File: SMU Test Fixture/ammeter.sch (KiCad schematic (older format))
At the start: 42 parts, among them K10 Integrator Reset, K5 3x Gain Enable, K6 Shunt Select, K7 Sense Select, K8 I/V Mode Select, K9 Shunt/Sense Select, U1 OPA189, U2 OPA551U, U3 OPA189, U4 OPA1611, U5 OPA192, U6 OPA192

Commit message: Add footprints for low precision/low power parts.
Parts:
- C1, C10, C11, C12, C13, C15, C2, C3, C4, C5, C6, C7, C8, C9: footprint (none) -> Capacitor_SMD:C_0805_2012Metric_Pad1.18x1.45mm_HandSolder
- R10, R12, R13, R14, R15, R16, R17, R18, R19, R8: footprint (none) -> Resistor_SMD:R_0805_2012Metric_Pad1.20x1.40mm_HandSolder
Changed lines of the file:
@@
 F 0 "C1" H 1092 946 50  0000 L CNN
 F 1 "100n" H 1092 855 50  0000 L CNN
-F 2 "" H 1000 900 50  0001 C CNN
+F 2 "Capacitor_SMD:C_0805_2012Metric_Pad1.18x1.45mm_HandSolder" H 1000 900 50  0001 C CNN
 F 3 "~" H 1000 900 50  0001 C CNN
 	1    1000 900
@@
 F 0 "C2" H 1092 1346 50  0000 L CNN
 F 1 "100n" H 1092 1255 50  0000 L CNN
-F 2 "" H 1000 1300 50  0001 C CNN
+F 2 "Capacitor_SMD:C_0805_2012Metric_Pad1.18x1.45mm_HandSolder" H 1000 1300 50  0001 C CNN
 F 3 "~" H 1000 1300 50  0001 C CNN
 	1    1000 1300
@@
 F 0 "R17" V 7895 3900 50  0000 C CNN
 F 1 "1M" V 7986 3900 50  0000 C CNN
-F 2 "" H 8100 3900 50  0001 C CNN
+F 2 "Resistor_SMD:R_0805_2012Metric_Pad1.20x1.40mm_HandSolder" H 8100 3900 50  0001 C CNN
 F 3 "~" H 8100 3900 50  0001 C CNN
 	1    8100 3900
@@
 F 0 "R16" V 7845 2450 50  0000 C CNN
 F 1 "1M" V 7936 2450 50  0000 C CNN
-F 2 "" H 8050 2450 50  0001 C CNN
+F 2 "Resistor_SMD:R_0805_2012Metric_Pad1.20x1.40mm_HandSolder" H 8050 2450 50  0001 C CNN
 F 3 "~" H 8050 2450 50  0001 C CNN
 	1    8050 2450
@@
 F 0 "R10" H 1700 3100 50  0000 C CNN
 F 1 "56K" H 1700 3000 50  0000 C CNN
-F 2 "" H 1800 3100 50  0001 C CNN
+F 2 "Resistor_SMD:R_0805_2012Metric_Pad1.20x1.40mm_HandSolder" H 1800 3100 50  0001 C CNN
 F 3 "~" H 1800 3100 50  0001 C CNN
 	1    1800 3100
@@
 F 0 "C13" H 2692 4046 50  0000 L CNN
 F 1 "33p" H 2692 3955 50  0000 L CNN
-F 2 "" H 2600 4000 50  0001 C CNN
+F 2 "Capacitor_SMD:C_0805_2012Metric_Pad1.18x1.45mm_HandSolder" H 2600 4000 50  0001 C CNN
 F 3 "~" H 2600 4000 50  0001 C CNN
 	1    2600 4000
@@
 F 0 "R8" V 945 4550 50  0000 C CNN
 F 1 "5.9K" V 1036 4550 50  0000 C CNN
-F 2 "" H 1150 4550 50  0001 C CNN
+F 2 "Resistor_SMD:R_0805_2012Metric_Pad1.20x1.40mm_HandSolder" H 1150 4550 50  0001 C CNN
 F 3 "~" H 1150 4550 50  0001 C CNN
 	1    1150 4550
@@
 F 0 "R12" V 3850 3800 50  0000 C CNN
 F 1 "11.8K" V 3636 3800 50  0000 C CNN
-F 2 "" H 3750 3800 50  0001 C CNN
+F 2 "Resistor_SMD:R_0805_2012Metric_Pad1.20x1.40mm_HandSolder" H 3750 3800 50  0001 C CNN
 F 3 "~" H 3750 3800 50  0001 C CNN
 	1    3750 3800
@@
 F 0 "R15" V 6845 5600 50  0000 C CNN
 F 1 "14.7K" V 6936 5600 50  0000 C CNN
-F 2 "" H 7050 5600 50  0001 C CNN
+F 2 "Resistor_SMD:R_0805_2012Metric_Pad1.20x1.40mm_HandSolder" H 7050 5600 50  0001 C CNN
 F 3 "~" H 7050 5600 50  0001 C CNN
 	1    7050 5600
@@
 F 0 "C15" V 6821 5950 50  0000 C CNN
 F 1 "6.2p" V 6912 5950 50  0000 C CNN
-F 2 "" H 7050 5950 50  0001 C CNN
+F 2 "Capacitor_SMD:C_0805_2012Metric_Pad1.18x1.45mm_HandSolder" H 7050 5950 50  0001 C CNN
 F 3 "~" H 7050 5950 50  0001 C CNN
 	1    7050 5950
@@
 F 0 "C3" H 1392 946 50  0000 L CNN
 F 1 "100n" H 1392 855 50  0000 L CNN
-F 2 "" H 1300 900 50  0001 C CNN
+F 2 "Capacitor_SMD:C_0805_2012Metric_Pad1.18x1.45mm_HandSolder" H 1300 900 50  0001 C CNN
 F 3 "~" H 1300 900 50  0001 C CNN
 	1    1300 900
@@
 F 0 "C5" H 1692 946 50  0000 L CNN
 F 1 "100n" H 1692 855 50  0000 L CNN
-F 2 "" H 1600 900 50  0001 C CNN
+F 2 "Capacitor_SMD:C_0805_2012Metric_Pad1.18x1.45mm_HandSolder" H 1600 900 50  0001 C CNN
 F 3 "~" H 1600 900 50  0001 C CNN
 	1    1600 900
@@
 F 0 "C7" H 1992 946 50  0000 L CNN
 F 1 "100n" H 1992 855 50  0000 L CNN
-F 2 "" H 1900 900 50  0001 C CNN
+F 2 "Capacitor_SMD:C_0805_2012Metric_Pad1.18x1.45mm_HandSolder" H 1900 900 50  0001 C CNN
 F 3 "~" H 1900 900 50  0001 C CNN
 	1    1900 900
@@
 F 0 "C9" H 2292 946 50  0000 L CNN
 F 1 "100n" H 2292 855 50  0000 L CNN
-F 2 "" H 2200 900 50  0001 C CNN
+F 2 "Capacitor_SMD:C_0805_2012Metric_Pad1.18x1.45mm_HandSolder" H 2200 900 50  0001 C CNN
 F 3 "~" H 2200 900 50  0001 C CNN
 	1    2200 900
@@
 F 0 "C11" H 2592 946 50  0000 L CNN
 F 1 "100n" H 2592 855 50  0000 L CNN
-F 2 "" H 2500 900 50  0001 C CNN
+F 2 "Capacitor_SMD:C_0805_2012Metric_Pad1.18x1.45mm_HandSolder" H 2500 900 50  0001 C CNN
 F 3 "~" H 2500 900 50  0001 C CNN
 	1    2500 900
@@
 F 0 "C4" H 1392 1346 50  0000 L CNN
 F 1 "100n" H 1392 1255 50  0000 L CNN
-F 2 "" H 1300 1300 50  0001 C CNN
+F 2 "Capacitor_SMD:C_0805_2012Metric_Pad1.18x1.45mm_HandSolder" H 1300 1300 50  0001 C CNN
 F 3 "~" H 1300 1300 50  0001 C CNN
 	1    1300 1300
@@
 F 0 "C6" H 1692 1346 50  0000 L CNN
 F 1 "100n" H 1692 1255 50  0000 L CNN
-F 2 "" H 1600 1300 50  0001 C CNN
+F 2 "Capacitor_SMD:C_0805_2012Metric_Pad1.18x1.45mm_HandSolder" H 1600 1300 50  0001 C CNN
 F 3 "~" H 1600 1300 50  0001 C CNN
 	1    1600 1300
@@
 F 0 "C8" H 1992 1346 50  0000 L CNN
 F 1 "100n" H 1992 1255 50  0000 L CNN
-F 2 "" H 1900 1300 50  0001 C CNN
+F 2 "Capacitor_SMD:C_0805_2012Metric_Pad1.18x1.45mm_HandSolder" H 1900 1300 50  0001 C CNN
 F 3 "~" H 1900 1300 50  0001 C CNN
 	1    1900 1300
@@
 F 0 "C10" H 2292 1346 50  0000 L CNN
 F 1 "100n" H 2292 1255 50  0000 L CNN
-F 2 "" H 2200 1300 50  0001 C CNN
+F 2 "Capacitor_SMD:C_0805_2012Metric_Pad1.18x1.45mm_HandSolder" H 2200 1300 50  0001 C CNN
 F 3 "~" H 2200 1300 50  0001 C CNN
 	1    2200 1300
@@
 F 0 "C12" H 2592 1346 50  0000 L CNN
 F 1 "100n" H 2592 1255 50  0000 L CNN
-F 2 "" H 2500 1300 50  0001 C CNN
+F 2 "Capacitor_SMD:C_0805_2012Metric_Pad1.18x1.45mm_HandSolder" H 2500 1300 50  0001 C CNN
 F 3 "~" H 2500 1300 50  0001 C CNN
 	1    2500 1300
@@
 F 0 "R18" V 9200 2300 50  0000 C CNN
 F 1 "5K" V 9400 2300 50  0000 C CNN
-F 2 "" H 9300 2300 50  0001 C CNN
+F 2 "Resistor_SMD:R_0805_2012Metric_Pad1.20x1.40mm_HandSolder" H 9300 2300 50  0001 C CNN
 F 3 "~" H 9300 2300 50  0001 C CNN
 	1    9300 2300
@@
 F 0 "R19" V 9250 3750 50  0000 C CNN
 F 1 "5K" V 9450 3750 50  0000 C CNN
-F 2 "" H 9350 3750 50  0001 C CNN
+F 2 "Resistor_SMD:R_0805_2012Metric_Pad1.20x1.40mm_HandSolder" H 9350 3750 50  0001 C CNN
 F 3 "~" H 9350 3750 50  0001 C CNN
 	1    9350 3750
@@
 F 0 "R14" V 5800 5950 50  0000 C CNN
 F 1 "150R" V 5900 5950 50  0000 C CNN
-F 2 "" H 6000 5950 50  0001 C CNN
+F 2 "Resistor_SMD:R_0805_2012Metric_Pad1.20x1.40mm_HandSolder" H 6000 5950 50  0001 C CNN
 F 3 "~" H 6000 5950 50  0001 C CNN
 	1    6000 5950
@@
 F 0 "R13" V 5800 5600 50  0000 C CNN
 F 1 "14.7K" V 5900 5600 50  0000 C CNN
-F 2 "" H 6000 5600 50  0001 C CNN
+F 2 "Resistor_SMD:R_0805_2012Metric_Pad1.20x1.40mm_HandSolder" H 6000 5600 50  0001 C CNN
 F 3 "~" H 6000 5600 50  0001 C CNN
 	1    6000 5600

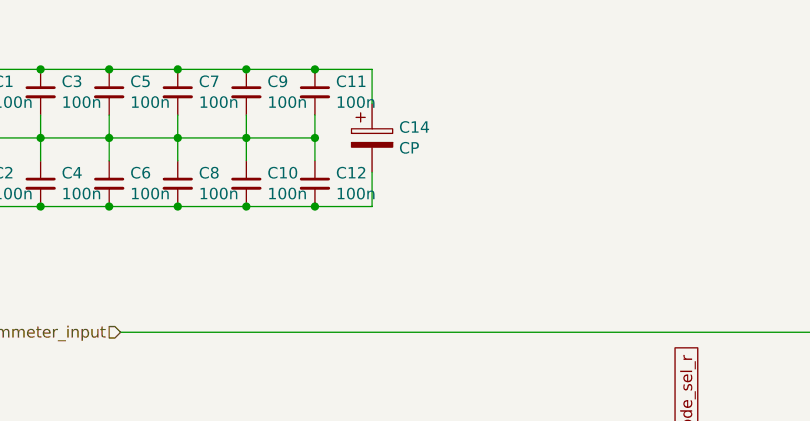
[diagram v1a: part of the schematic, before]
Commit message: More footprints added.
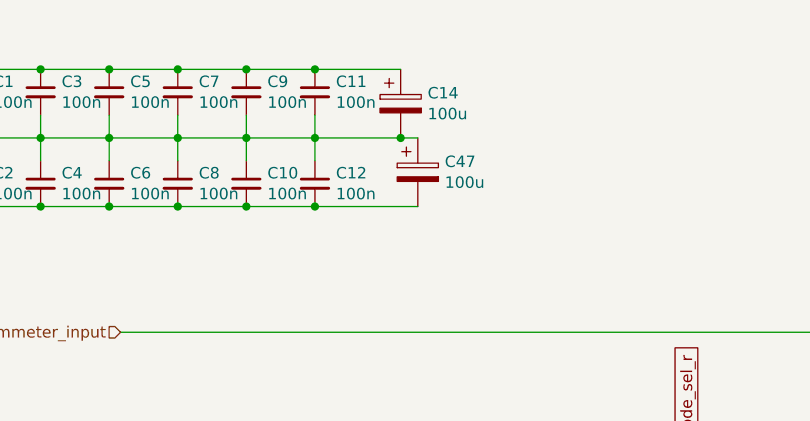
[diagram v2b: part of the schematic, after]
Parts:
- added C47: 100u, Capacitor_SMD:CP_Elec_8x10, symbol Device:CP
- C14: value CP -> 100u; footprint (none) -> Capacitor_SMD:CP_Elec_8x10; PN (none) -> UCD1V101MNL1GS
- C15: footprint Capacitor_SMD:C_0805_2012Metric_Pad1.18x1.45mm_HandSolder -> Capacitor_SMD:C_0603_1608Metric_Pad1.08x0.95mm_HandSolder; PN (none) -> GRM0335C1H6R2BA01D
- C16, C17: footprint (none) -> Capacitor_THT:C_Rect_L18.0mm_W11.0mm_P15.00mm_FKS3_FKP3; PN (none) -> ECW-FD2W105JC
- R11: footprint (none) -> Resistor_SMD:R_0805_2012Metric_Pad1.20x1.40mm_HandSolder; PN (none) -> ERA-6ARW103V
- R13, R15: footprint Resistor_SMD:R_0805_2012Metric_Pad1.20x1.40mm_HandSolder -> Resistor_SMD:R_1206_3216Metric_Pad1.30x1.75mm_HandSolder; PN (none) -> ERA-8ARW1472V
- R14: footprint Resistor_SMD:R_0805_2012Metric_Pad1.20x1.40mm_HandSolder -> Resistor_SMD:R_0603_1608Metric_Pad0.98x0.95mm_HandSolder; PN (none) -> RG1608N-151-W-T1
- R7: footprint (none) -> eaton:CSM_Vishay_Shunt_4term; PN (none) -> Y14870R01000B9R
- R9: footprint (none) -> Resistor_SMD:R_0805_2012Metric_Pad1.20x1.40mm_HandSolder; PN (none) -> RNCF0805AKT10R0
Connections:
- net -15V: now also C47.2; no longer C14.2
- net GND: now also C14.2, C47.1
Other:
- moved on the sheet: C14
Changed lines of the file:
@@
 F 0 "R11" H 2000 6200 50  0000 L CNN
 F 1 "10K" H 2000 6100 50  0000 L CNN
-F 2 "" H 1950 5850 50  0001 C CNN
+F 2 "Resistor_SMD:R_0805_2012Metric_Pad1.20x1.40mm_HandSolder" H 1950 5850 50  0001 C CNN
 F 3 "~" H 1950 5850 50  0001 C CNN
+F 4 " ERA-6ARW103V" H 1950 5850 50  0001 C CNN "PN"
 	1    1950 5850
 	-1   0    0    -1
@@
 F 0 "R9" H 1500 6200 50  0000 L CNN
 F 1 "10R" H 1500 6100 50  0000 L CNN
-F 2 "" H 1450 5850 50  0001 C CNN
+F 2 "Resistor_SMD:R_0805_2012Metric_Pad1.20x1.40mm_HandSolder" H 1450 5850 50  0001 C CNN
 F 3 "~" H 1450 5850 50  0001 C CNN
+F 4 "RNCF0805AKT10R0" H 1450 5850 50  0001 C CNN "PN"
 	1    1450 5850
 	-1   0    0    -1
@@
 F 0 "C17" V 8450 3300 50  0000 C CNN
 F 1 "1u" V 8650 3300 50  0000 C CNN
-F 2 "" H 8550 3300 50  0001 C CNN
+F 2 "Capacitor_THT:C_Rect_L18.0mm_W11.0mm_P15.00mm_FKS3_FKP3" H 8550 3300 50  0001 C CNN
 F 3 "~" H 8550 3300 50  0001 C CNN
+F 4 " ECW-FD2W105JC " V 8550 3300 50  0001 C CNN "PN"
 	1    8550 3300
 	0    1    1    0
@@
 F 0 "R7" H 1250 6300 50  0000 R CNN
 F 1 "0R01" H 1300 6200 50  0000 R CNN
-F 2 "" V 1030 5900 50  0001 C CNN
+F 2 "eaton:CSM_Vishay_Shunt_4term" V 1030 5900 50  0001 C CNN
 F 3 "~" H 1100 5900 50  0001 C CNN
+F 4 "Y14870R01000B9R" H 1100 5900 50  0001 C CNN "PN"
 	1    1100 5900
 	-1   0    0    -1
@@
 F 0 "R15" V 6845 5600 50  0000 C CNN
 F 1 "14.7K" V 6936 5600 50  0000 C CNN
-F 2 "Resistor_SMD:R_0805_2012Metric_Pad1.20x1.40mm_HandSolder" H 7050 5600 50  0001 C CNN
+F 2 "Resistor_SMD:R_1206_3216Metric_Pad1.30x1.75mm_HandSolder" H 7050 5600 50  0001 C CNN
 F 3 "~" H 7050 5600 50  0001 C CNN
+F 4 "ERA-8ARW1472V" V 7050 5600 50  0001 C CNN "PN"
 	1    7050 5600
 	0    1    1    0
@@
 F 0 "C15" V 6821 5950 50  0000 C CNN
 F 1 "6.2p" V 6912 5950 50  0000 C CNN
-F 2 "Capacitor_SMD:C_0805_2012Metric_Pad1.18x1.45mm_HandSolder" H 7050 5950 50  0001 C CNN
+F 2 "Capacitor_SMD:C_0603_1608Metric_Pad1.08x0.95mm_HandSolder" H 7050 5950 50  0001 C CNN
 F 3 "~" H 7050 5950 50  0001 C CNN
+F 4 "GRM0335C1H6R2BA01D" V 7050 5950 50  0001 C CNN "PN"
 	1    7050 5950
 	0    1    1    0
@@
 F 0 "C16" V 8400 1850 50  0000 C CNN
 F 1 "1u" V 8600 1850 50  0000 C CNN
-F 2 "" H 8500 1850 50  0001 C CNN
+F 2 "Capacitor_THT:C_Rect_L18.0mm_W11.0mm_P15.00mm_FKS3_FKP3" H 8500 1850 50  0001 C CNN
 F 3 "~" H 8500 1850 50  0001 C CNN
+F 4 " ECW-FD2W105JC " V 8500 1850 50  0001 C CNN "PN"
 	1    8500 1850
 	0    1    1    0
@@
 L Device:CP C14
 U 1 1 60ECEBF3
-P 2750 1100
-F 0 "C14" H 2868 1146 50  0000 L CNN
-F 1 "CP" H 2868 1055 50  0000 L CNN
-F 2 "" H 2788 950 50  0001 C CNN
-F 3 "~" H 2750 1100 50  0001 C CNN
-	1    2750 1100
-	1    0    0    -1
-$EndComp
-Wire Wire Line
-	2750 800  2750 950
-Wire Wire Line
-	2750 1400 2750 1250
+P 2875 950
+F 0 "C14" H 2993 996 50  0000 L CNN
+F 1 "100u" H 2993 905 50  0000 L CNN
+F 2 "Capacitor_SMD:CP_Elec_8x10" H 2913 800 50  0001 C CNN
+F 3 "~" H 2875 950 50  0001 C CNN
+F 4 "UCD1V101MNL1GS" H 2875 950 50  0001 C CNN "PN"
+	1    2875 950
+	1    0    0    -1
+$EndComp
 Wire Wire Line
 	1000 800  1300 800
@@
 $EndComp
 Connection ~ 2500 800
-Wire Wire Line
-	2500 800  2750 800
 $Comp
 L Device:C_Small C4
@@
 $EndComp
 Connection ~ 2500 1400
-Wire Wire Line
-	2500 1400 2750 1400
 $Comp
 L power:-15V #PWR012
@@
 F 0 "R14" V 5800 5950 50  0000 C CNN
 F 1 "150R" V 5900 5950 50  0000 C CNN
-F 2 "Resistor_SMD:R_0805_2012Metric_Pad1.20x1.40mm_HandSolder" H 6000 5950 50  0001 C CNN
+F 2 "Resistor_SMD:R_0603_1608Metric_Pad0.98x0.95mm_HandSolder" H 6000 5950 50  0001 C CNN
 F 3 "~" H 6000 5950 50  0001 C CNN
+F 4 "RG1608N-151-W-T1" V 6000 5950 50  0001 C CNN "PN"
 	1    6000 5950
 	0    1    1    0
@@
 F 0 "R13" V 5800 5600 50  0000 C CNN
 F 1 "14.7K" V 5900 5600 50  0000 C CNN
-F 2 "Resistor_SMD:R_0805_2012Metric_Pad1.20x1.40mm_HandSolder" H 6000 5600 50  0001 C CNN
+F 2 "Resistor_SMD:R_1206_3216Metric_Pad1.30x1.75mm_HandSolder" H 6000 5600 50  0001 C CNN
 F 3 "~" H 6000 5600 50  0001 C CNN
+F 4 "ERA-8ARW1472V" V 6000 5600 50  0001 C CNN "PN"
 	1    6000 5600
 	0    1    1    0
@@
 	1    0    0    -1
 $EndComp
+$Comp
+L Device:CP C47
+U 1 1 6014511A
+P 2950 1250
+F 0 "C47" H 3068 1296 50  0000 L CNN
+F 1 "100u" H 3068 1205 50  0000 L CNN
+F 2 "Capacitor_SMD:CP_Elec_8x10" H 2988 1100 50  0001 C CNN
+F 3 "~" H 2950 1250 50  0001 C CNN
+F 4 "UCD1V101MNL1GS" H 2950 1250 50  0001 C CNN "PN"
+	1    2950 1250
+	1    0    0    -1
+$EndComp
+Wire Wire Line
+	2500 1400 2950 1400
+Wire Wire Line
+	2500 1100 2875 1100
+Wire Wire Line
+	2875 1100 2950 1100
+Connection ~ 2875 1100
+Wire Wire Line
+	2500 800  2875 800
 $EndSCHEMATC

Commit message: Footprint updates
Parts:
- C1, C10, C11, C12, C2, C3, C4, C5, C6, C7, C8, C9: footprint Capacitor_SMD:C_0805_2012Metric_Pad1.18x1.45mm_HandSolder -> Capacitor_SMD:C_1206_3216Metric_Pad1.33x1.80mm_HandSolder; PN (none) -> CGA5L2C0G1H104J160AA
- C13: footprint Capacitor_SMD:C_0805_2012Metric_Pad1.18x1.45mm_HandSolder -> Capacitor_SMD:C_0201_0603Metric_Pad0.64x0.40mm_HandSolder; PN (none) -> GRM0335C1H330FA01D
- R10: PN (none) -> CRCW080556K0JNEA
- R12: PN (none) -> RQ73C2A11K8BTDF
- R16, R17: footprint Resistor_SMD:R_0805_2012Metric_Pad1.20x1.40mm_HandSolder -> Resistor_SMD:R_1206_3216Metric_Pad1.30x1.75mm_HandSolder; PN (none) -> RG3216N-1004-W-T1
- R18, R19: PN (none) -> CRCW08055K00JNTA
- R8: PN (none) -> RN73C2A5K9BTDF
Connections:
- net +15V: now also C2.1, C4.1, C6.1; no longer C11.1, C7.1, C9.1
- net -15V: now also C11.2, C7.2, C9.2; no longer C2.2, C4.2, C6.2
- net GND: now also C11.1, C2.2, C4.2, C6.2, C7.1, C9.1; no longer C11.2, C2.1, C4.1, C6.1, C7.2, C9.2
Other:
- moved on the sheet: C14, C47

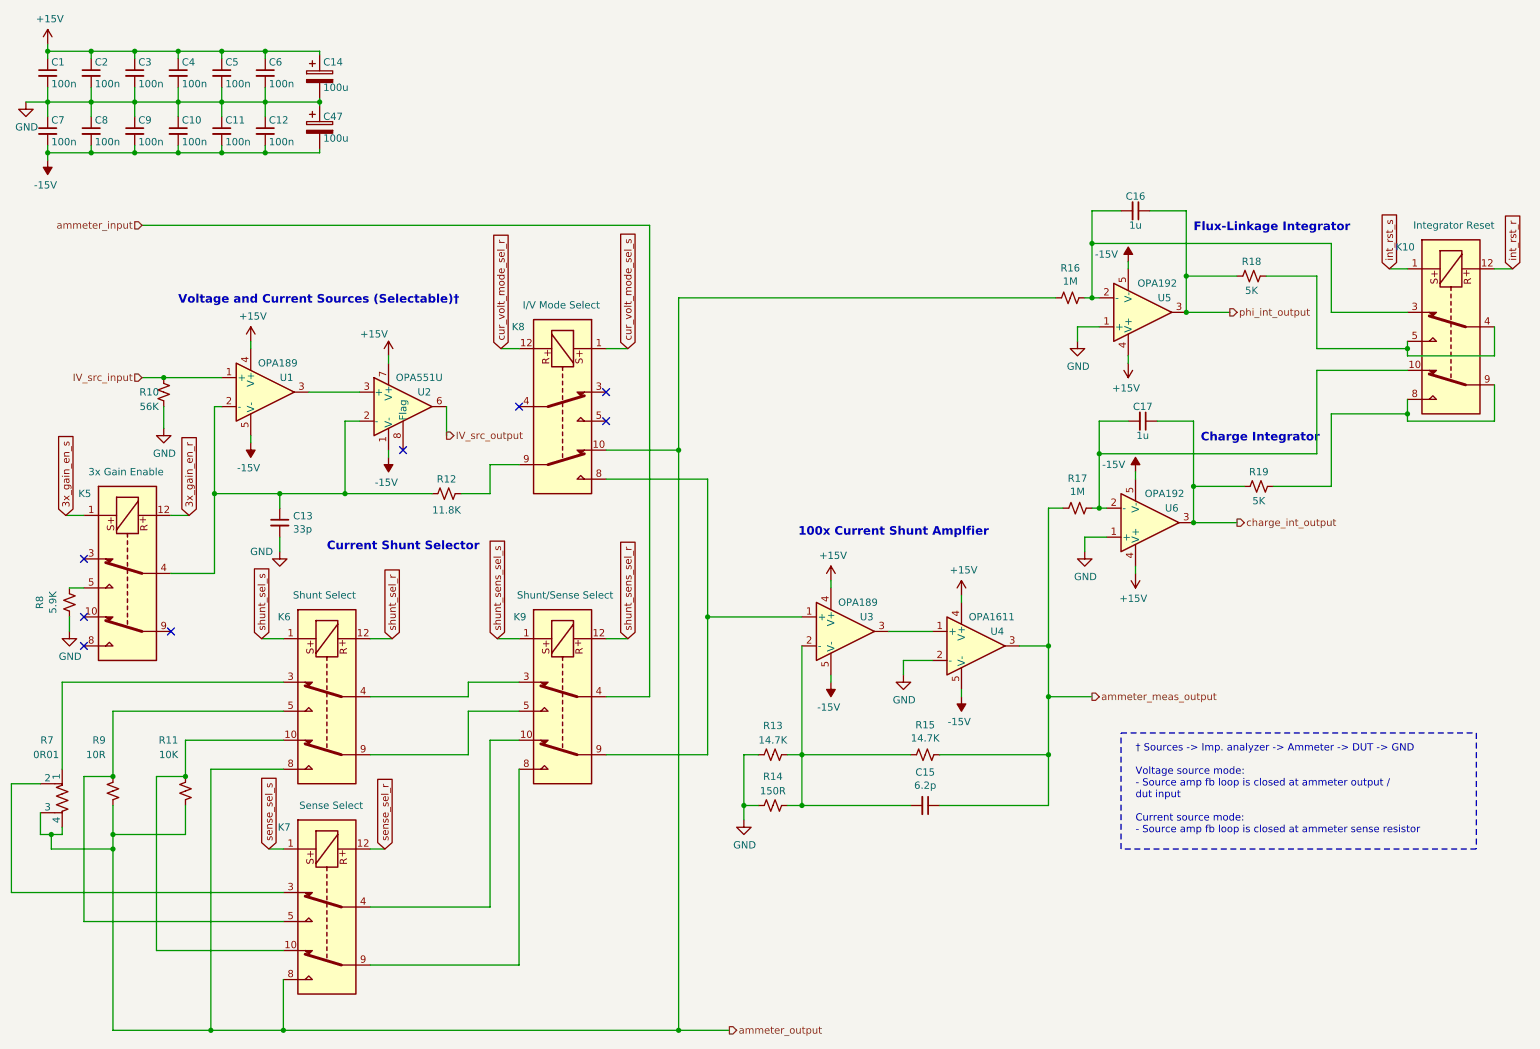
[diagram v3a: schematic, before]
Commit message: Switch to 28V txfrmr, nix preregs, nix 5V for AD2, switch to 12V relay power.
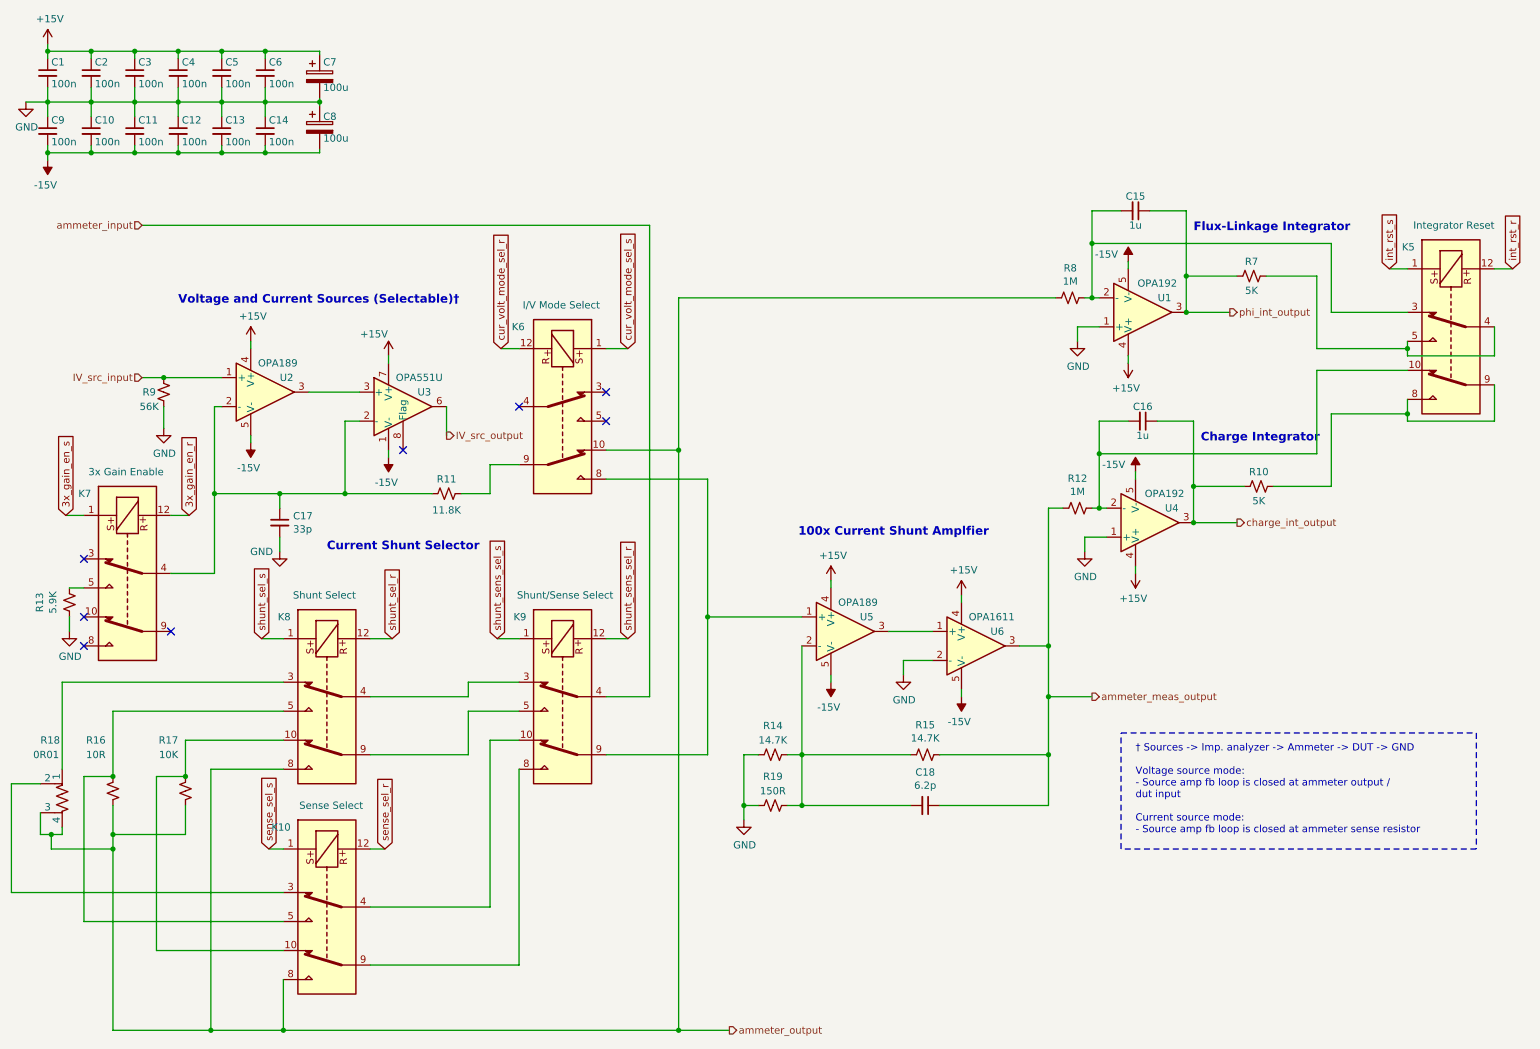
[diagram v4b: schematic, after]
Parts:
- renumbered C8 to C10, C9 to C11, C10 to C12, C11 to C13, C12 to C14, C16 to C15, C17 to C16, C13 to C17, C15 to C18, C14 to C7, C47 to C8, C7 to C9, K7 to K10, K10 to K5, K8 to K6, K5 to K7, K6 to K8, R19 to R10, R12 to R11, R17 to R12, R8 to R13, R13 to R14, R9 to R16, R11 to R17, R7 to R18, R14 to R19, R18 to R7, R16 to R8, R10 to R9, U5 to U1, U1 to U2, U2 to U3, U6 to U4, U3 to U5, U4 to U6

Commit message: Reannotate, power supply schematic improvements, begin power supply layout.
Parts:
- R18: footprint eaton:CSM_Vishay_Shunt_4term -> MAGI_Footprints:CSM_Vishay_Shunt_4term
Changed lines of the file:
@@
 F 0 "R18" H 1250 6300 50  0000 R CNN
 F 1 "0R01" H 1300 6200 50  0000 R CNN
-F 2 "eaton:CSM_Vishay_Shunt_4term" V 1030 5900 50  0001 C CNN
+F 2 "MAGI_Footprints:CSM_Vishay_Shunt_4term" V 1030 5900 50  0001 C CNN
 F 3 "~" H 1100 5900 50  0001 C CNN
 F 4 "Y14870R01000B9R" H 1100 5900 50  0001 C CNN "PN"
